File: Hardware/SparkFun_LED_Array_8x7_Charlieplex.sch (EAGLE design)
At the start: 73 parts

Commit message: Layout complete.
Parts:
- FRAME1: value FRAME-LETTER -> (none); DESIGNER (none) -> Shawn Hymel
- JP1: device SparkFun-Connectors:M08LOCK -> SparkFun-Connectors:M08LOCK_NO_SILK
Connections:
- net N$1: now also JP1.4; no longer JP1.5
- net N$2: now also JP1.5; no longer JP1.4
- net N$3: now also JP1.6; no longer JP1.3
- net N$4: now also JP1.7; no longer JP1.2
- net N$5: now also JP1.8; no longer JP1.1
- net N$6: now also JP1.3; no longer JP1.6
- net N$7: now also JP1.2; no longer JP1.7
- net N$8: now also JP1.1; no longer JP1.8
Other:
- note removed: "v01"
- moved on the sheet: JP1
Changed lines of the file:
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@@
 <setting verticaltext="up"/>
 </settings>
-<grid distance="0.1" unitdist="inch" unit="inch" style="lines" multiple="1" display="yes" altdistance="0.01" altunitdist="inch" altunit="inch"/>
+<grid distance="0.1" unitdist="inch" unit="inch" style="lines" multiple="1" display="no" altdistance="0.01" altunitdist="inch" altunit="inch"/>
 <layers>
 <layer number="1" name="Top" color="4" fill="1" visible="no" active="no"/>
@@
 </classes>
 <parts>
-<part name="FRAME1" library="SparkFun-Aesthetics" deviceset="FRAME-LETTER" device=""/>
-<part name="JP1" library="SparkFun-Connectors" deviceset="M08" device="LOCK"/>
+<part name="FRAME1" library="SparkFun-Aesthetics" deviceset="FRAME-LETTER" device="">
+<attribute name="DESIGNER" value="Shawn Hymel"/>
+</part>
 <part name="R1" library="SparkFun-Resistors" deviceset="RESISTOR" device="0603-RES" value="33">
 <attribute name="PROD_ID" value="RES-08270"/>
@@
 <part name="LOGO2" library="SparkFun-Aesthetics" deviceset="OSHW-LOGO" device="S"/>
 <part name="U$1" library="SparkFun-Aesthetics" deviceset="SFE_LOGO_NAME_FLAME" device=".1_INCH"/>
+<part name="JP1" library="SparkFun-Connectors" deviceset="M08" device="LOCK_NO_SILK"/>
 </parts>
 <sheets>
 <sheet>
 <plain>
-<text x="238.76" y="7.62" size="2.54" layer="94">v01</text>
 <text x="167.64" y="11.176" size="2.54" layer="94">Shawn Hymel</text>
 </plain>
 <instances>
 <instance part="FRAME1" gate="G$1" x="0" y="0"/>
-<instance part="FRAME1" gate="G$2" x="147.32" y="0"/>
-<instance part="JP1" gate="G$1" x="27.94" y="114.3" rot="MR180"/>
+<instance part="FRAME1" gate="V" x="147.32" y="0"/>
 <instance part="R1" gate="G$1" x="50.8" y="132.08" smashed="yes">
 <attribute name="PROD_ID" x="50.8" y="132.08" size="1.778" layer="96" display="off"/>
@@
 <instance part="LOGO2" gate="G$1" x="73.66" y="10.16"/>
 <instance part="U$1" gate="G$1" x="88.9" y="2.54"/>
+<instance part="JP1" gate="G$1" x="27.94" y="111.76"/>
 </instances>
 <busses>
@@
 <net name="N$1" class="0">
 <segment>
-<pinref part="JP1" gate="G$1" pin="5"/>
 <wire x1="33.02" y1="111.76" x2="45.72" y2="111.76" width="0.1524" layer="91"/>
 <pinref part="R5" gate="G$1" pin="1"/>
+<pinref part="JP1" gate="G$1" pin="4"/>
 </segment>
 </net>
 <net name="N$2" class="0">
 <segment>
-<pinref part="JP1" gate="G$1" pin="4"/>
 <wire x1="33.02" y1="114.3" x2="43.18" y2="114.3" width="0.1524" layer="91"/>
 <wire x1="43.18" y1="114.3" x2="43.18" y2="116.84" width="0.1524" layer="91"/>
 <wire x1="43.18" y1="116.84" x2="45.72" y2="116.84" width="0.1524" layer="91"/>
 <pinref part="R4" gate="G$1" pin="1"/>
+<pinref part="JP1" gate="G$1" pin="5"/>
 </segment>
 </net>
 <net name="N$3" class="0">
 <segment>
-<pinref part="JP1" gate="G$1" pin="3"/>
 <wire x1="33.02" y1="116.84" x2="40.64" y2="116.84" width="0.1524" layer="91"/>
 <wire x1="40.64" y1="116.84" x2="40.64" y2="121.92" width="0.1524" layer="91"/>
 <wire x1="40.64" y1="121.92" x2="45.72" y2="121.92" width="0.1524" layer="91"/>
 <pinref part="R3" gate="G$1" pin="1"/>
+<pinref part="JP1" gate="G$1" pin="6"/>
 </segment>
 </net>
 <net name="N$4" class="0">
 <segment>
-<pinref part="JP1" gate="G$1" pin="2"/>
 <wire x1="33.02" y1="119.38" x2="38.1" y2="119.38" width="0.1524" layer="91"/>
 <wire x1="38.1" y1="119.38" x2="38.1" y2="127" width="0.1524" layer="91"/>
 <wire x1="38.1" y1="127" x2="45.72" y2="127" width="0.1524" layer="91"/>
 <pinref part="R2" gate="G$1" pin="1"/>
+<pinref part="JP1" gate="G$1" pin="7"/>
 </segment>
 </net>
 <net name="N$5" class="0">
 <segment>
-<pinref part="JP1" gate="G$1" pin="1"/>
 <wire x1="33.02" y1="121.92" x2="35.56" y2="121.92" width="0.1524" layer="91"/>
 <wire x1="35.56" y1="121.92" x2="35.56" y2="132.08" width="0.1524" layer="91"/>
 <pinref part="R1" gate="G$1" pin="1"/>
 <wire x1="35.56" y1="132.08" x2="45.72" y2="132.08" width="0.1524" layer="91"/>
+<pinref part="JP1" gate="G$1" pin="8"/>
 </segment>
 </net>
 <net name="N$6" class="0">
 <segment>
-<pinref part="JP1" gate="G$1" pin="6"/>
 <wire x1="33.02" y1="109.22" x2="43.18" y2="109.22" width="0.1524" layer="91"/>
 <wire x1="43.18" y1="109.22" x2="43.18" y2="106.68" width="0.1524" layer="91"/>
 <wire x1="43.18" y1="106.68" x2="45.72" y2="106.68" width="0.1524" layer="91"/>
 <pinref part="R6" gate="G$1" pin="1"/>
+<pinref part="JP1" gate="G$1" pin="3"/>
 </segment>
 </net>
 <net name="N$7" class="0">
 <segment>
-<pinref part="JP1" gate="G$1" pin="7"/>
 <wire x1="33.02" y1="106.68" x2="40.64" y2="106.68" width="0.1524" layer="91"/>
 <wire x1="40.64" y1="106.68" x2="40.64" y2="101.6" width="0.1524" layer="91"/>
 <wire x1="40.64" y1="101.6" x2="45.72" y2="101.6" width="0.1524" layer="91"/>
 <pinref part="R7" gate="G$1" pin="1"/>
+<pinref part="JP1" gate="G$1" pin="2"/>
 </segment>
 </net>
 <net name="N$8" class="0">
 <segment>
-<pinref part="JP1" gate="G$1" pin="8"/>
 <wire x1="33.02" y1="104.14" x2="38.1" y2="104.14" width="0.1524" layer="91"/>
 <wire x1="38.1" y1="104.14" x2="38.1" y2="96.52" width="0.1524" layer="91"/>
 <wire x1="38.1" y1="96.52" x2="45.72" y2="96.52" width="0.1524" layer="91"/>
 <pinref part="R8" gate="G$1" pin="1"/>
-</segment>
-</net>
+<pinref part="JP1" gate="G$1" pin="1"/>
+</segment>
+</net>

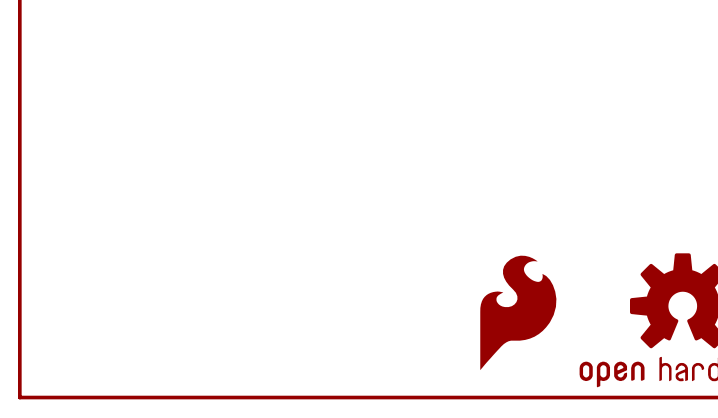
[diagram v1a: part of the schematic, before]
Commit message: Added BadgerHack logo. Moved some vias to make room.
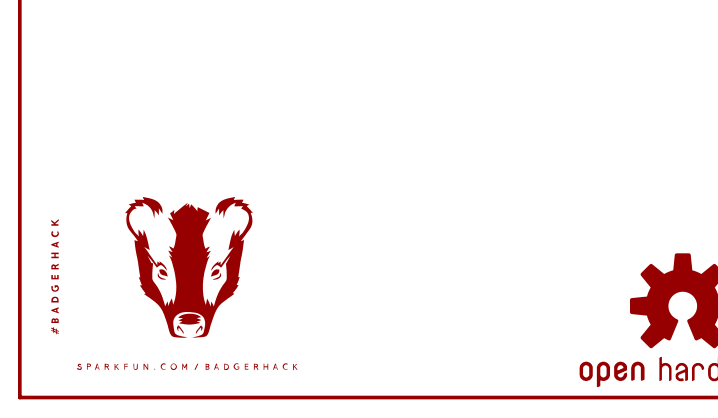
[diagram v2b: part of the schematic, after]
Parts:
- removed LOGO1: SFE_LOGO_FLAME.1_INCH, SparkFun-Aesthetics:SFE_LOGO_FLAME.1_INCH
- added U$2: BADGERHACK_LOGO, SparkFun-Aesthetics:BADGERHACK_LOGO
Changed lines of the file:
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@@
 <part name="STANDOFF1" library="SparkFun-Electromechanical" deviceset="STAND-OFF" device=""/>
 <part name="STANDOFF2" library="SparkFun-Electromechanical" deviceset="STAND-OFF" device=""/>
-<part name="LOGO1" library="SparkFun-Aesthetics" deviceset="SFE_LOGO_FLAME" device=".1_INCH"/>
 <part name="LOGO2" library="SparkFun-Aesthetics" deviceset="OSHW-LOGO" device="S"/>
 <part name="U$1" library="SparkFun-Aesthetics" deviceset="SFE_LOGO_NAME_FLAME" device=".1_INCH"/>
 <part name="JP1" library="SparkFun-Connectors" deviceset="M08" device="LOCK_NO_SILK"/>
+<part name="U$2" library="SparkFun-Aesthetics" deviceset="BADGERHACK_LOGO" device=""/>
 </parts>
 <sheets>
@@
 <instance part="STANDOFF1" gate="G$1" x="241.3" y="33.02"/>
 <instance part="STANDOFF2" gate="G$1" x="241.3" y="27.94"/>
-<instance part="LOGO1" gate="G$1" x="50.8" y="2.54"/>
 <instance part="LOGO2" gate="G$1" x="73.66" y="10.16"/>
 <instance part="U$1" gate="G$1" x="88.9" y="2.54"/>
 <instance part="JP1" gate="G$1" x="27.94" y="111.76"/>
+<instance part="U$2" gate="G$1" x="2.54" y="2.54"/>
 </instances>
 <busses>

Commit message: Changed badger silk to separate components.
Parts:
- U$2: value BADGERHACK_LOGO -> BADGERHACK_LOGODUMMY; device SparkFun-Aesthetics:BADGERHACK_LOGO -> SparkFun-Aesthetics:BADGERHACK_LOGODUMMY
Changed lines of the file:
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@@
 <setting verticaltext="up"/>
 </settings>
-<grid distance="0.1" unitdist="inch" unit="inch" style="lines" multiple="1" display="no" altdistance="0.01" altunitdist="inch" altunit="inch"/>
+<grid distance="0.1" unitdist="inch" unit="inch" style="lines" multiple="1" display="yes" altdistance="0.01" altunitdist="inch" altunit="inch"/>
 <layers>
 <layer number="1" name="Top" color="4" fill="1" visible="no" active="no"/>
@@
 <part name="U$1" library="SparkFun-Aesthetics" deviceset="SFE_LOGO_NAME_FLAME" device=".1_INCH"/>
 <part name="JP1" library="SparkFun-Connectors" deviceset="M08" device="LOCK_NO_SILK"/>
-<part name="U$2" library="SparkFun-Aesthetics" deviceset="BADGERHACK_LOGO" device=""/>
+<part name="U$2" library="SparkFun-Aesthetics" deviceset="BADGERHACK_LOGO" device="DUMMY"/>
 </parts>
 <sheets>

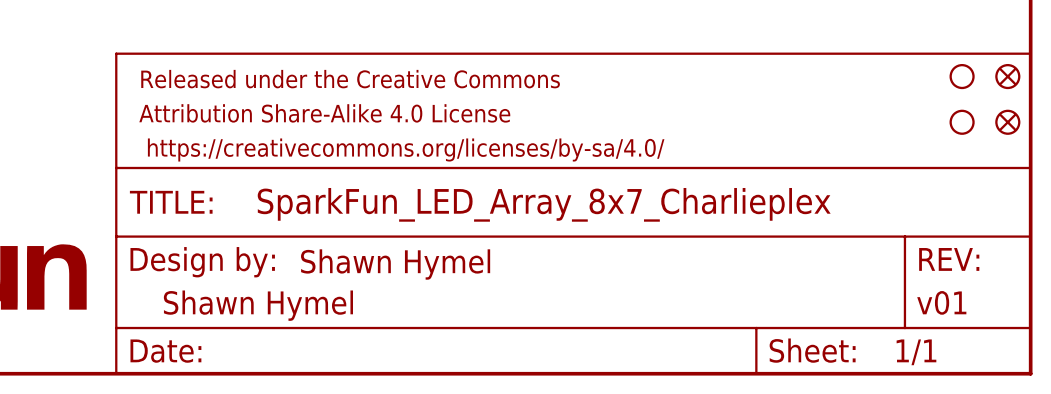
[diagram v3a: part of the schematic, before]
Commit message: Flipped all silk screen on bottom of board. Switched top and bottom silk pin numbers. Flipped order of pin numbers to line up with the Interactive Badge.
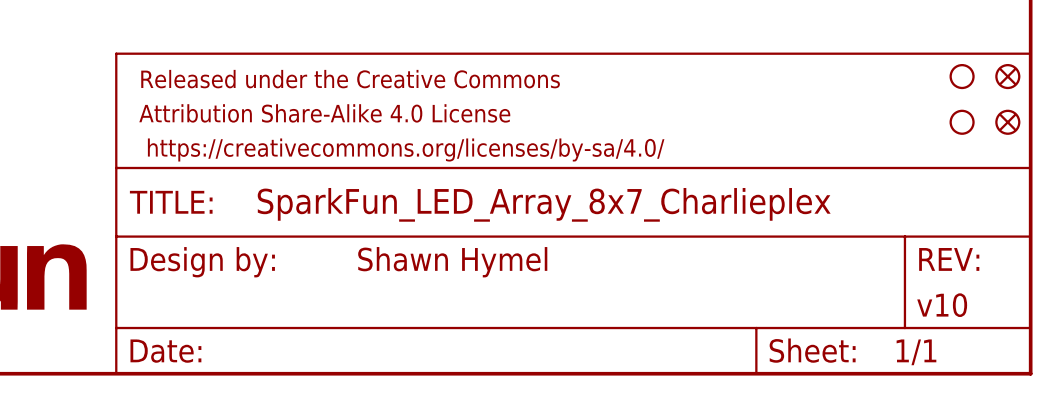
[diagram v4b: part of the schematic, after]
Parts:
- FRAME1: VERSION (none) -> v10
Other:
- note removed: "Shawn Hymel"
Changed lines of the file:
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@@
 <setting verticaltext="up"/>
 </settings>
-<grid distance="0.1" unitdist="inch" unit="inch" style="lines" multiple="1" display="yes" altdistance="0.01" altunitdist="inch" altunit="inch"/>
+<grid distance="0.1" unitdist="inch" unit="inch" style="lines" multiple="1" display="no" altdistance="0.01" altunitdist="inch" altunit="inch"/>
 <layers>
 <layer number="1" name="Top" color="4" fill="1" visible="no" active="no"/>
@@
 <part name="FRAME1" library="SparkFun-Aesthetics" deviceset="FRAME-LETTER" device="">
 <attribute name="DESIGNER" value="Shawn Hymel"/>
+<attribute name="VERSION" value="v10"/>
 </part>
 <part name="R1" library="SparkFun-Resistors" deviceset="RESISTOR" device="0603-RES" value="33">
@@
 <sheet>
 <plain>
-<text x="167.64" y="11.176" size="2.54" layer="94">Shawn Hymel</text>
 </plain>
 <instances>
